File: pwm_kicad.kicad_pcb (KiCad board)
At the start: 2 copper layers, 50 x 47 mm, 29 parts, among them J1 Screw_Terminal_01x03, Q1 BC547, Q2 BC557, Q3 BS170, Q4 BC547, Q5 BC557, Q6 BS170, U1 TLC274, U2 PC817, U3 PC817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

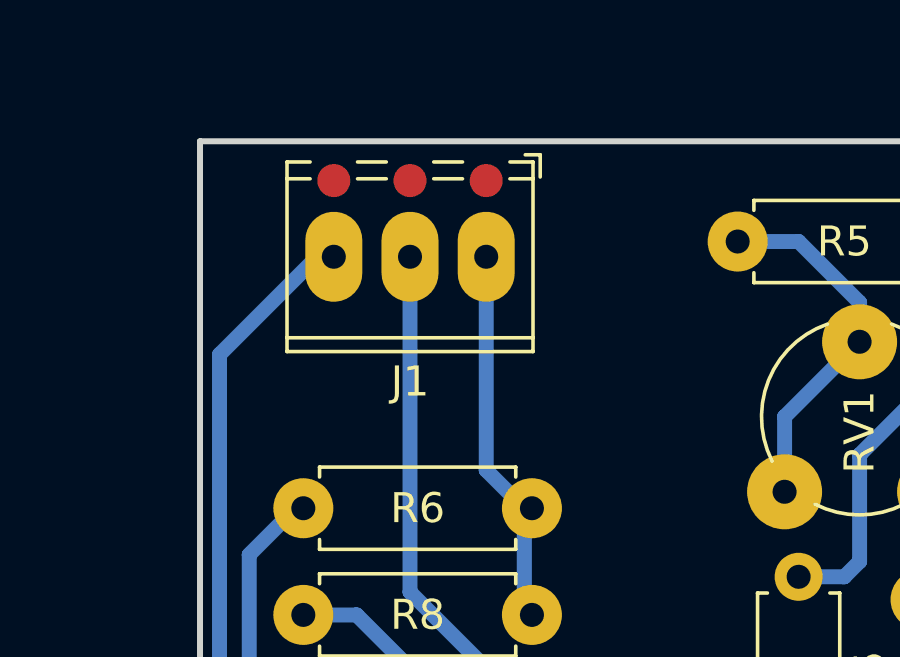
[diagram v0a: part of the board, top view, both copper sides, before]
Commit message: Update pwm_kicad.kicad_pcb
Added silkscreen for terminals
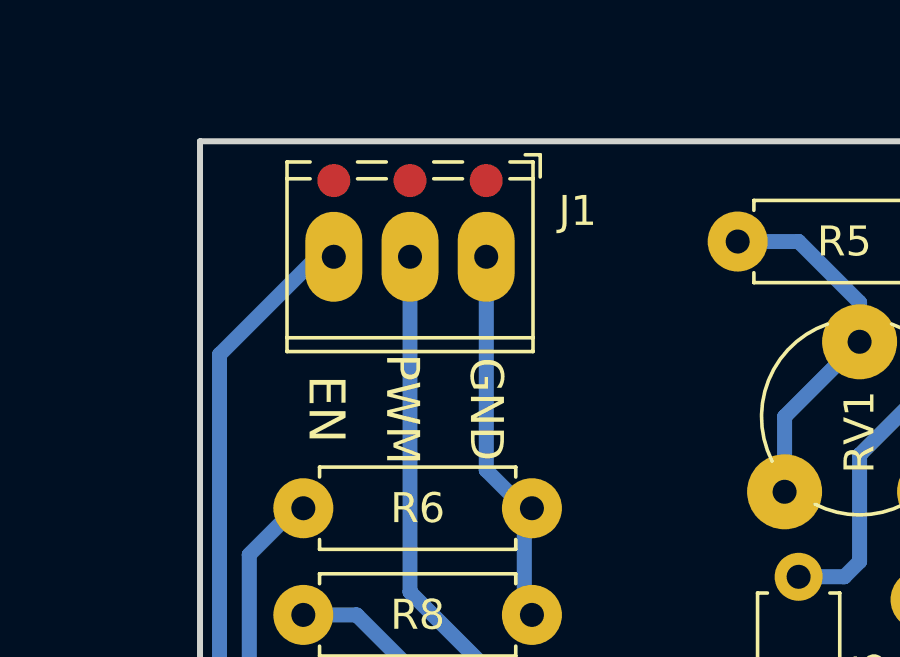
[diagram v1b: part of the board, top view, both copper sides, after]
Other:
- board text added: "EN"
- board text added: "GND"
- board text added: "PWM"
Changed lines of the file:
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@@
     (property "Sheetname" "")
     (attr through_hole)
-    (fp_text reference "J1" (at 2.54 -4.16) (layer "F.SilkS")
+    (fp_text reference "J1" (at -3.048 1.524) (layer "F.SilkS")
       (effects (font (size 1 1) (thickness 0.15)))
     )
@@
       (effects (font (size 1 1) (thickness 0.15)))
     )
-    (fp_text value "220" (at 3.81 2.37) (layer "F.Fab")
+    (fp_text value "220" (at -2.794 0) (layer "F.Fab")
       (effects (font (size 1 1) (thickness 0.15)))
     )
@@
       (effects (font (size 1 1) (thickness 0.15)))
     )
-    (fp_text value "220" (at 3.81 2.37) (layer "F.Fab")
+    (fp_text value "220" (at -2.794 0) (layer "F.Fab")
       (effects (font (size 1 1) (thickness 0.15)))
     )
@@
   )
   (gr_rect (start 120 66) (end 170 113) (layer "Edge.Cuts") (width 0.2) (fill none))
+  (gr_text "GND" (at 129.54 74.93 270) (layer "F.SilkS")
+    (effects (font (size 1.1 1.1) (thickness 0.2)))
+  )
+  (gr_text "EN" (at 124.206 74.93 270) (layer "F.SilkS")
+    (effects (font (size 1.2 1.2) (thickness 0.2)))
+  )
+  (gr_text "PWM" (at 126.746 74.93 270) (layer "F.SilkS")
+    (effects (font (size 1.1 1.1) (thickness 0.2)))
+  )
   (segment (start 141.986 85.852) (end 138.780882 85.852) (width 0.5) (layer "B.Cu") (net 1))
   (segment (start 142.08 90.33) (end 144.018 88.392) (width 0.5) (layer "B.Cu") (net 1))
